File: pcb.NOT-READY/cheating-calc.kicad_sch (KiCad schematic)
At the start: 22 parts, among them J1 Conn_01x04, J2 Conn_01x04, Q1 MMBF170, Q2 MMBF170, U1 ESP32-C3-MINI-1-N4, U2 TLV75533PDBVR, U3 TLV75533PDQNR, U4 TLV75533PDRVR

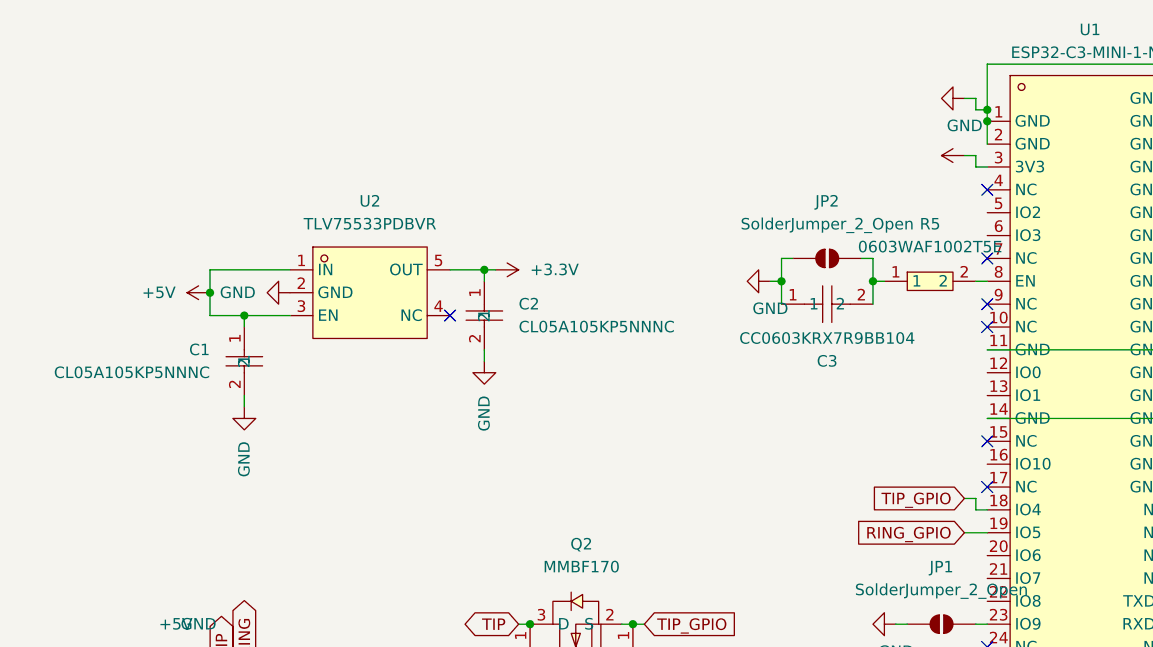
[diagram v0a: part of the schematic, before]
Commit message: Update regulator chip and remove rounded versions
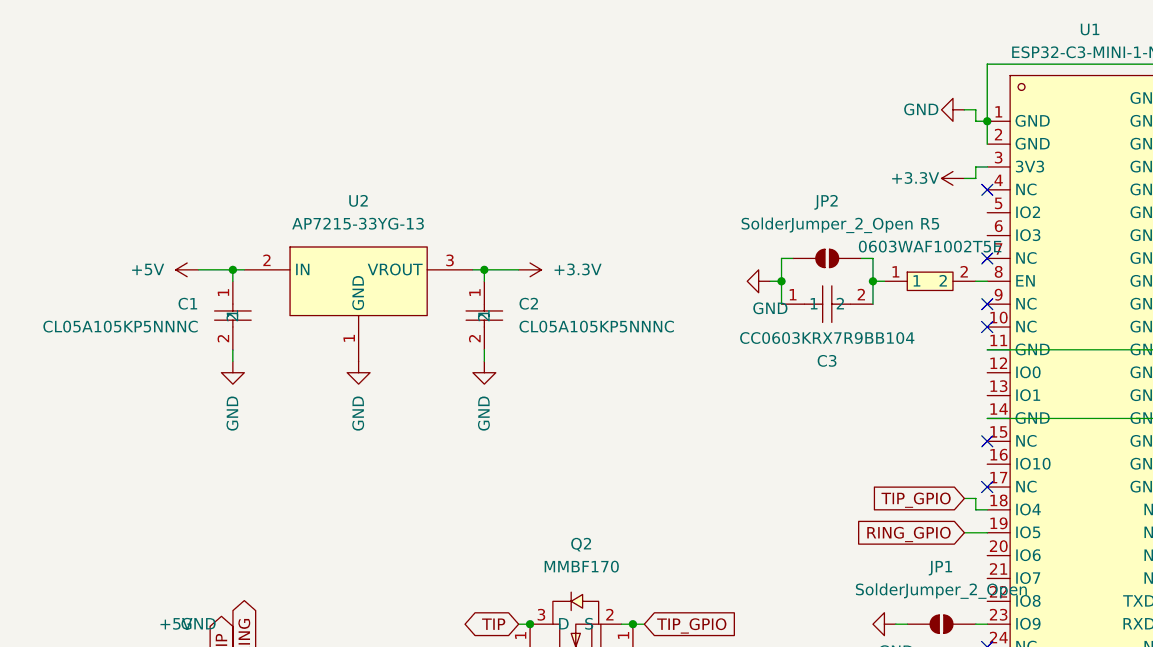
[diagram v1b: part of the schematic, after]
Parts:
- removed U2: TLV75533PDBVR, easyeda2kicad:SOT-23-5_L3.0-W1.7-P0.95-LS2.8-BR, symbol easyeda2kicad:TLV75533PDBVR
- added U2: AP7215-33YG-13, easyeda2kicad:SOT-89-3_L4.5-W2.5-P1.50-LS4.2-BR, symbol easyeda2kicad:AP7215-33YG-13
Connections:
- net +3.3V: now also U2.3 (VROUT)
- net +5V: now also U2.2 (IN)
- net GND: now also U2.1 (GND)
- no-connect marks 19 -> 18
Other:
- moved on the sheet: C1
